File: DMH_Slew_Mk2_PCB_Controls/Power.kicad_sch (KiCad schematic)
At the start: 13 parts, among them J0 Conn_01x01, J100 IDC_02x08, J200 IDC_02x05, U10 LM4040LP-10

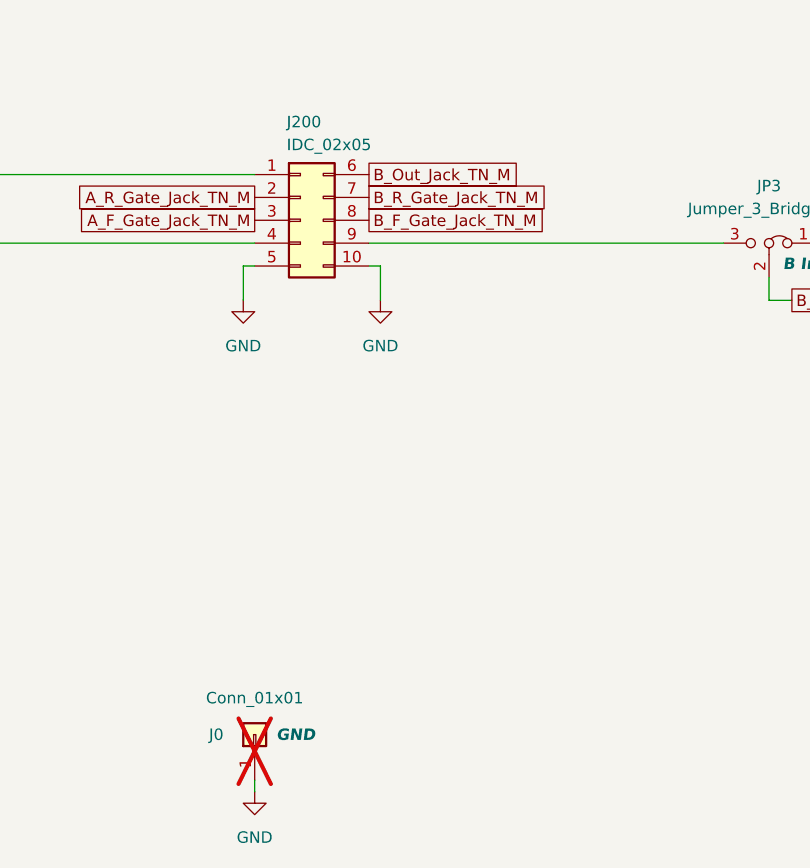
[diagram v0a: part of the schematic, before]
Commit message: Designed Controls PCB
... and removed Mod feature
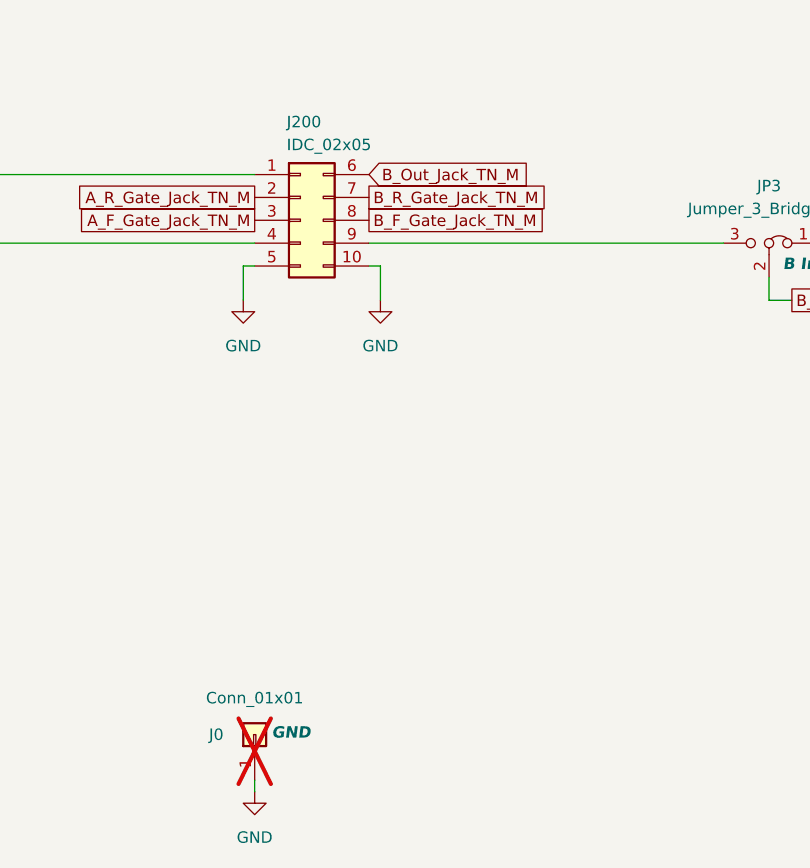
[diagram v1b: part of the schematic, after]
